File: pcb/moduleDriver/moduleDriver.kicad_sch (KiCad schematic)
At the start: 44 parts, among them J1 MOTOR, J10 Sensor, J11 Power, J12 Power, J13 Power, J14 LOOPBACK, J2 MOTOR, J3 MOTOR, J4 MOTOR, J5 IDC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

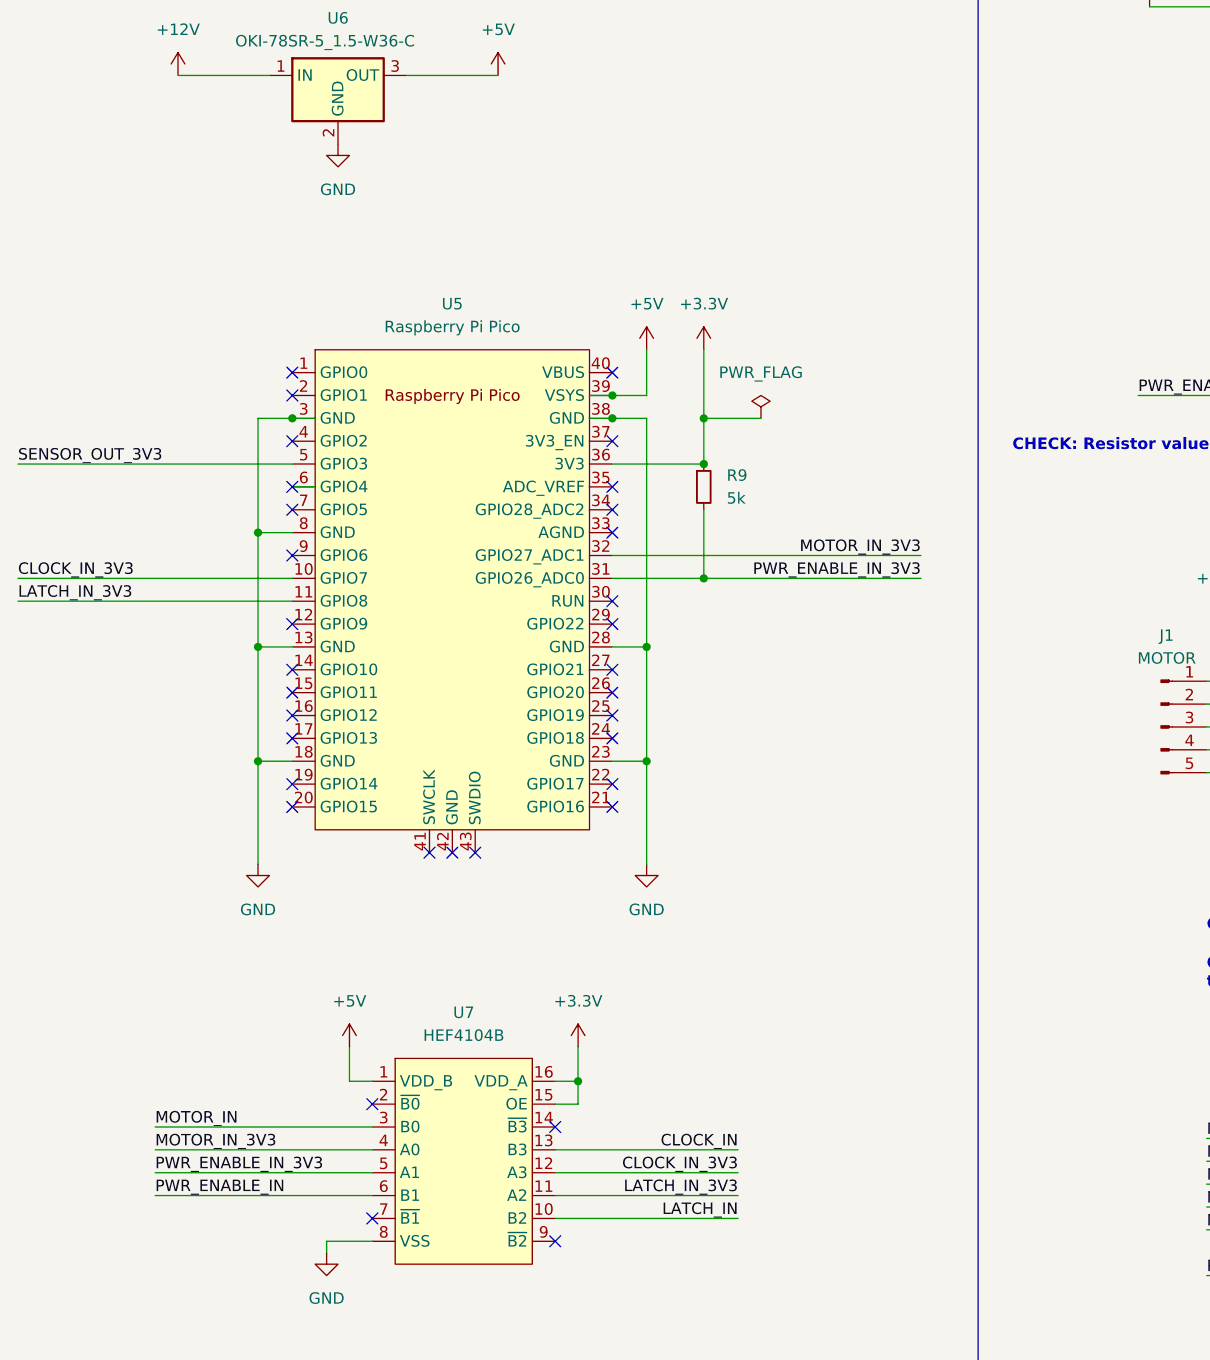
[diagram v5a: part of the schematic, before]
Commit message: Rework pico layout
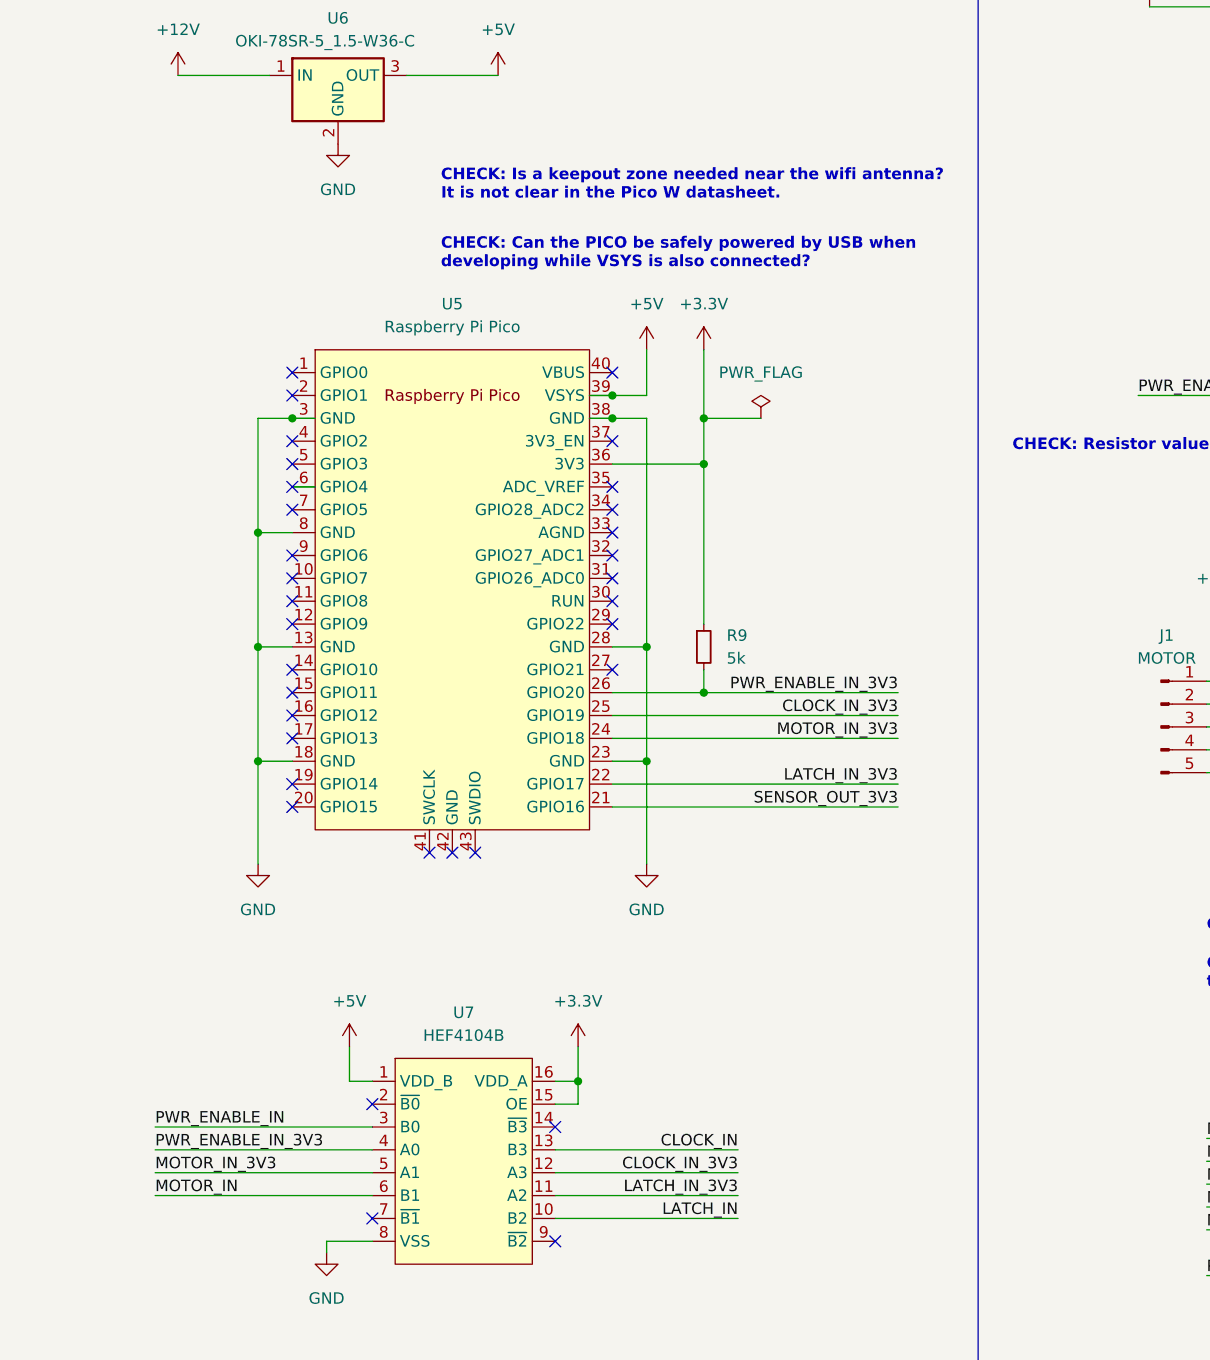
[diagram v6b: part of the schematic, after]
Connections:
- net CLOCK_IN_3V3: now also U5.25 (GPIO19); no longer U5.10 (GPIO7)
- net LATCH_IN_3V3: now also U5.22 (GPIO17); no longer U5.11 (GPIO8)
- net MOTOR_IN: now also U7.6 (B1); no longer U7.3 (B0)
- net MOTOR_IN_3V3: now also U5.24 (GPIO18), U7.5 (A1); no longer U5.32 (GPIO27_ADC1), U7.4 (A0)
- net PWR_ENABLE_IN: now also U7.3 (B0); no longer U7.6 (B1)
- net PWR_ENABLE_IN_3V3: now also U5.26 (GPIO20), U7.4 (A0); no longer U5.31 (GPIO26_ADC0), U7.5 (A1)
- net SENSOR_OUT_3V3: now also U5.21 (GPIO16); no longer U5.5 (GPIO3)
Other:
- note added: "CHECK: Can the PICO be safely powered by USB when developing while VSYS is also connected?"
- note added: "CHECK: Is a keepout zone needed near the wifi antenna? It is not clear in the Pico W datasheet."
- moved on the sheet: R9
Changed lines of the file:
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@@
   (junction (at 226.06 252.73) (diameter 0) (color 0 0 0 0)
   )
-  (junction (at 91.44 123.19) (diameter 0) (color 0 0 0 0)
-  )
   (junction (at 212.09 59.69) (diameter 0) (color 0 0 0 0)
   )
@@
   )
   (junction (at 374.65 92.71) (diameter 0) (color 0 0 0 0)
+  )
+  (junction (at 91.44 135.89) (diameter 0) (color 0 0 0 0)
   )
   (junction (at 45.72 105.41) (diameter 0) (color 0 0 0 0)
@@
   (no_connect (at 81.28 133.35))
   (no_connect (at 81.28 128.27))
+  (no_connect (at 81.28 123.19))
   (no_connect (at 45.72 148.59))
   (no_connect (at 74.93 196.85))
@@
   (no_connect (at 45.72 133.35))
   (no_connect (at 66.04 153.67))
+  (no_connect (at 45.72 123.19))
   (no_connect (at 297.18 66.04))
   (no_connect (at 45.72 113.03))
+  (no_connect (at 45.72 125.73))
   (no_connect (at 81.28 100.33))
   (no_connect (at 297.18 71.12))
@@
   (no_connect (at 45.72 135.89))
   (no_connect (at 60.96 153.67))
-  (no_connect (at 81.28 140.97))
   (no_connect (at 45.72 107.95))
   (no_connect (at 297.18 63.5))
@@
   (no_connect (at 81.28 115.57))
   (no_connect (at 322.58 53.34))
-  (no_connect (at 81.28 146.05))
   (no_connect (at 45.72 128.27))
   (no_connect (at 45.72 120.65))
-  (no_connect (at 81.28 138.43))
+  (no_connect (at 45.72 110.49))
   (no_connect (at 81.28 107.95))
-  (no_connect (at 81.28 135.89))
-  (no_connect (at 81.28 148.59))
   (no_connect (at 81.28 125.73))
+  (no_connect (at 81.28 120.65))
   (wire (pts (xy 281.94 50.8) (xy 297.18 50.8))
     (stroke (width 0) (type default) (color 0 0 0 0))
@@
     (stroke (width 0) (type default) (color 0 0 0 0))
   )
-  (wire (pts (xy 81.28 120.65) (xy 115.57 120.65))
+  (wire (pts (xy 81.28 140.97) (xy 113.03 140.97))
     (stroke (width 0) (type default) (color 0 0 0 0))
   )
@@
     (stroke (width 0) (type default) (color 0 0 0 0))
   )
-  (wire (pts (xy 81.28 123.19) (xy 91.44 123.19))
+  (wire (pts (xy 81.28 135.89) (xy 91.44 135.89))
     (stroke (width 0) (type default) (color 0 0 0 0))
   )
@@
     (stroke (width 0) (type default) (color 0 0 0 0))
   )
+  (wire (pts (xy 91.44 128.27) (xy 91.44 110.49))
+    (stroke (width 0) (type default) (color 0 0 0 0))
+  )
   (wire (pts (xy 372.11 76.2) (xy 372.11 81.28))
     (stroke (width 0) (type default) (color 0 0 0 0))
@@
     (stroke (width 0) (type default) (color 0 0 0 0))
   )
-  (wire (pts (xy 91.44 123.19) (xy 115.57 123.19))
+  (wire (pts (xy 91.44 135.89) (xy 113.03 135.89))
     (stroke (width 0) (type default) (color 0 0 0 0))
   )
@@
     (stroke (width 0) (type default) (color 0 0 0 0))
   )
-  (wire (pts (xy 15.24 110.49) (xy 45.72 110.49))
+  (wire (pts (xy 81.28 148.59) (xy 113.03 148.59))
     (stroke (width 0) (type default) (color 0 0 0 0))
   )
@@
     (stroke (width 0) (type default) (color 0 0 0 0))
   )
-  (wire (pts (xy 15.24 125.73) (xy 45.72 125.73))
+  (wire (pts (xy 81.28 146.05) (xy 113.03 146.05))
     (stroke (width 0) (type default) (color 0 0 0 0))
   )
@@
     (stroke (width 0) (type default) (color 0 0 0 0))
   )
-  (wire (pts (xy 15.24 123.19) (xy 45.72 123.19))
+  (wire (pts (xy 81.28 138.43) (xy 113.03 138.43))
     (stroke (width 0) (type default) (color 0 0 0 0))
   )
@@
     (stroke (width 0) (type default) (color 0 0 0 0))
   )
-  (wire (pts (xy 91.44 115.57) (xy 91.44 123.19))
+  (wire (pts (xy 91.44 133.35) (xy 91.44 135.89))
     (stroke (width 0) (type default) (color 0 0 0 0))
   )
@@
     (effects (font (size 1.27 1.27) bold) (justify left bottom))
   )
+  (text "CHECK: Is a keepout zone needed near the wifi antenna?\nIt is not clear in the Pico W datasheet."
+    (at 62.23 81.28 0)
+    (effects (font (size 1.27 1.27) bold) (justify left bottom))
+  )
   (text "CHECK: Any recommendations on thermal vias (see Google Doc)\n"
     (at 147.32 162.56 0)
     (effects (font (size 1.27 1.27) (thickness 0.254) bold) (justify left bottom))
   )
+  (text "CHECK: Can the PICO be safely powered by USB when\ndeveloping while VSYS is also connected?"
+    (at 62.23 88.9 0)
+    (effects (font (size 1.27 1.27) bold) (justify left bottom))
+  )
   (text "PCB is designed for the 3d printed split flap display:\nhttps://www.printables.com/model/69464-split-flap-display\n\nEach PCB can power four modules. Modules can be chained\ntogether to build larger displays"
     (at 25.4 34.29 0)
@@
     (effects (font (size 1.27 1.27)) (justify right bottom))
   )
-  (label "MOTOR_IN_3V3" (at 115.57 120.65 180)
+  (label "MOTOR_IN_3V3" (at 113.03 140.97 180)
     (effects (font (size 1.27 1.27)) (justify right bottom))
   )
@@
     (effects (font (size 1.27 1.27)) (justify left bottom))
   )
-  (label "PWR_ENABLE_IN_3V3" (at 115.57 123.19 180)
+  (label "PWR_ENABLE_IN_3V3" (at 113.03 135.89 180)
     (effects (font (size 1.27 1.27)) (justify right bottom))
   )
@@
     (effects (font (size 1.27 1.27)) (justify right bottom))
   )
-  (label "MOTOR_IN_3V3" (at 30.48 186.69 0)
+  (label "MOTOR_IN_3V3" (at 30.48 189.23 0)
     (effects (font (size 1.27 1.27)) (justify left bottom))
   )
@@
     (effects (font (size 1.27 1.27)) (justify left bottom))
   )
-  (label "PWR_ENABLE_IN" (at 30.48 191.77 0)
-    (effects (font (size 1.27 1.27)) (justify left bottom))
-  )
-  (label "LATCH_IN_3V3" (at 15.24 125.73 0)
-    (effects (font (size 1.27 1.27)) (justify left bottom))
+  (label "PWR_ENABLE_IN" (at 30.48 184.15 0)
+    (effects (font (size 1.27 1.27)) (justify left bottom))
+  )
+  (label "LATCH_IN_3V3" (at 113.03 146.05 180)
+    (effects (font (size 1.27 1.27)) (justify right bottom))
   )
   (label "SENSOR_IN" (at 241.3 250.19 0)
@@
     (effects (font (size 1.27 1.27)) (justify left bottom))
   )
-  (label "SENSOR_OUT_3V3" (at 15.24 110.49 0)
-    (effects (font (size 1.27 1.27)) (justify left bottom))
+  (label "SENSOR_OUT_3V3" (at 113.03 148.59 180)
+    (effects (font (size 1.27 1.27)) (justify right bottom))
   )
   (label "SENSOR_A" (at 351.79 45.72 0)
@@
     (effects (font (size 1.27 1.27)) (justify left bottom))
   )
-  (label "CLOCK_IN_3V3" (at 15.24 123.19 0)
-    (effects (font (size 1.27 1.27)) (justify left bottom))
+  (label "CLOCK_IN_3V3" (at 113.03 138.43 180)
+    (effects (font (size 1.27 1.27)) (justify right bottom))
   )
   (label "PWR_ENABLE_OUT" (at 190.5 252.73 0)
@@
     (effects (font (size 1.27 1.27)) (justify right bottom))
   )
-  (label "PWR_ENABLE_IN_3V3" (at 30.48 189.23 0)
+  (label "PWR_ENABLE_IN_3V3" (at 30.48 186.69 0)
     (effects (font (size 1.27 1.27)) (justify left bottom))
   )
@@
     (effects (font (size 1.27 1.27)) (justify left bottom))
   )
-  (label "MOTOR_IN" (at 30.48 184.15 0)
+  (label "MOTOR_IN" (at 30.48 191.77 0)
     (effects (font (size 1.27 1.27)) (justify left bottom))
   )
@@
     (pin "5")
   )
-  (symbol (lib_id "Device:R_Small") (at 91.44 113.03 0) (unit 1)
+  (symbol (lib_id "Device:R_Small") (at 91.44 130.81 0) (unit 1)
     (in_bom yes) (on_board yes) (fields_autoplaced)
-    (property "Reference" "R9" (id 0) (at 93.98 111.7599 0)
+    (property "Reference" "R9" (id 0) (at 93.98 129.5399 0)
       (effects (font (size 1.27 1.27)) (justify left))
     )
-    (property "Value" "5k" (id 1) (at 93.98 114.2999 0)
+    (property "Value" "5k" (id 1) (at 93.98 132.0799 0)
       (effects (font (size 1.27 1.27)) (justify left))
     )
-    (property "Footprint" "Resistor_SMD:R_0603_1608Metric" (id 2) (at 91.44 113.03 0)
-      (effects (font (size 1.27 1.27)) hide)
-    )
-    (property "Datasheet" "~" (id 3) (at 91.44 113.03 0)
-      (effects (font (size 1.27 1.27)) hide)
-    )
+    (property "Footprint" "Resistor_SMD:R_0603_1608Metric" (id 2) (at 91.44 130.81 0)
+      (effects (font (size 1.27 1.27)) hide)
+    )
+    (property "Datasheet" "~" (id 3) (at 91.44 130.81 0)
+      (effects (font (size 1.27 1.27)) hide)
+    )
